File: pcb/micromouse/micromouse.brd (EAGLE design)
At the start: 80 x 115 mm, 66 parts, among them IC1 LM2575-5.0WU-(TR), IC2 LM2575-3.3WU-(TR), IC3 DSPIC33FJ64MC804-PT, IC4 L293D, Y1 7.3728MHz

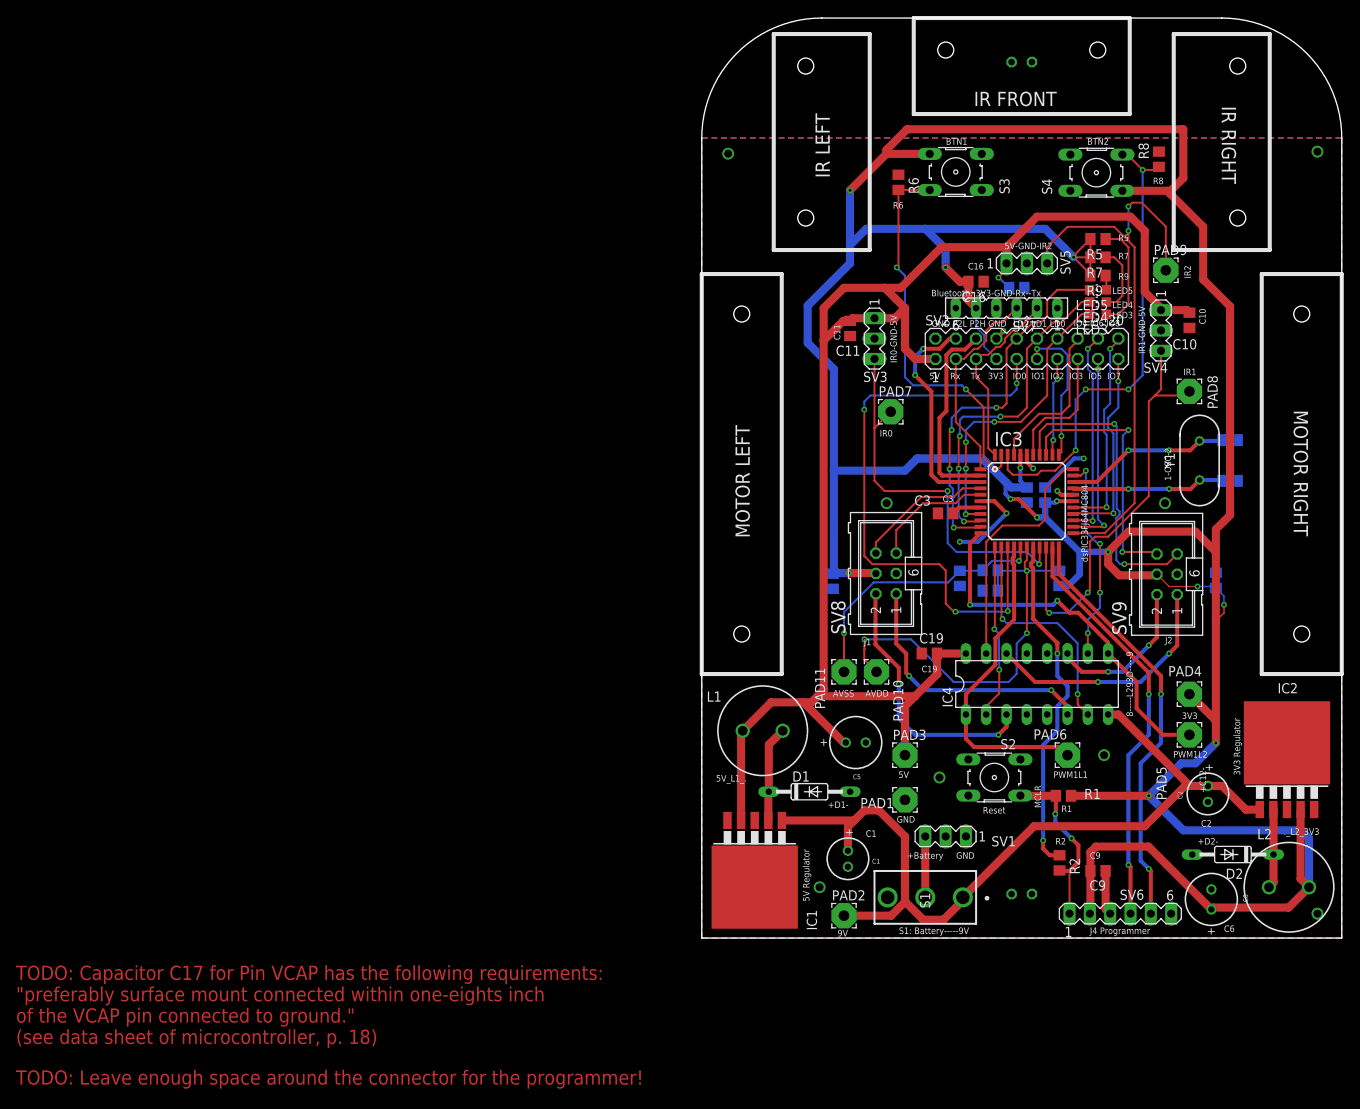
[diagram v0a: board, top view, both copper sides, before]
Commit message: Fix positioning of motor connectors.
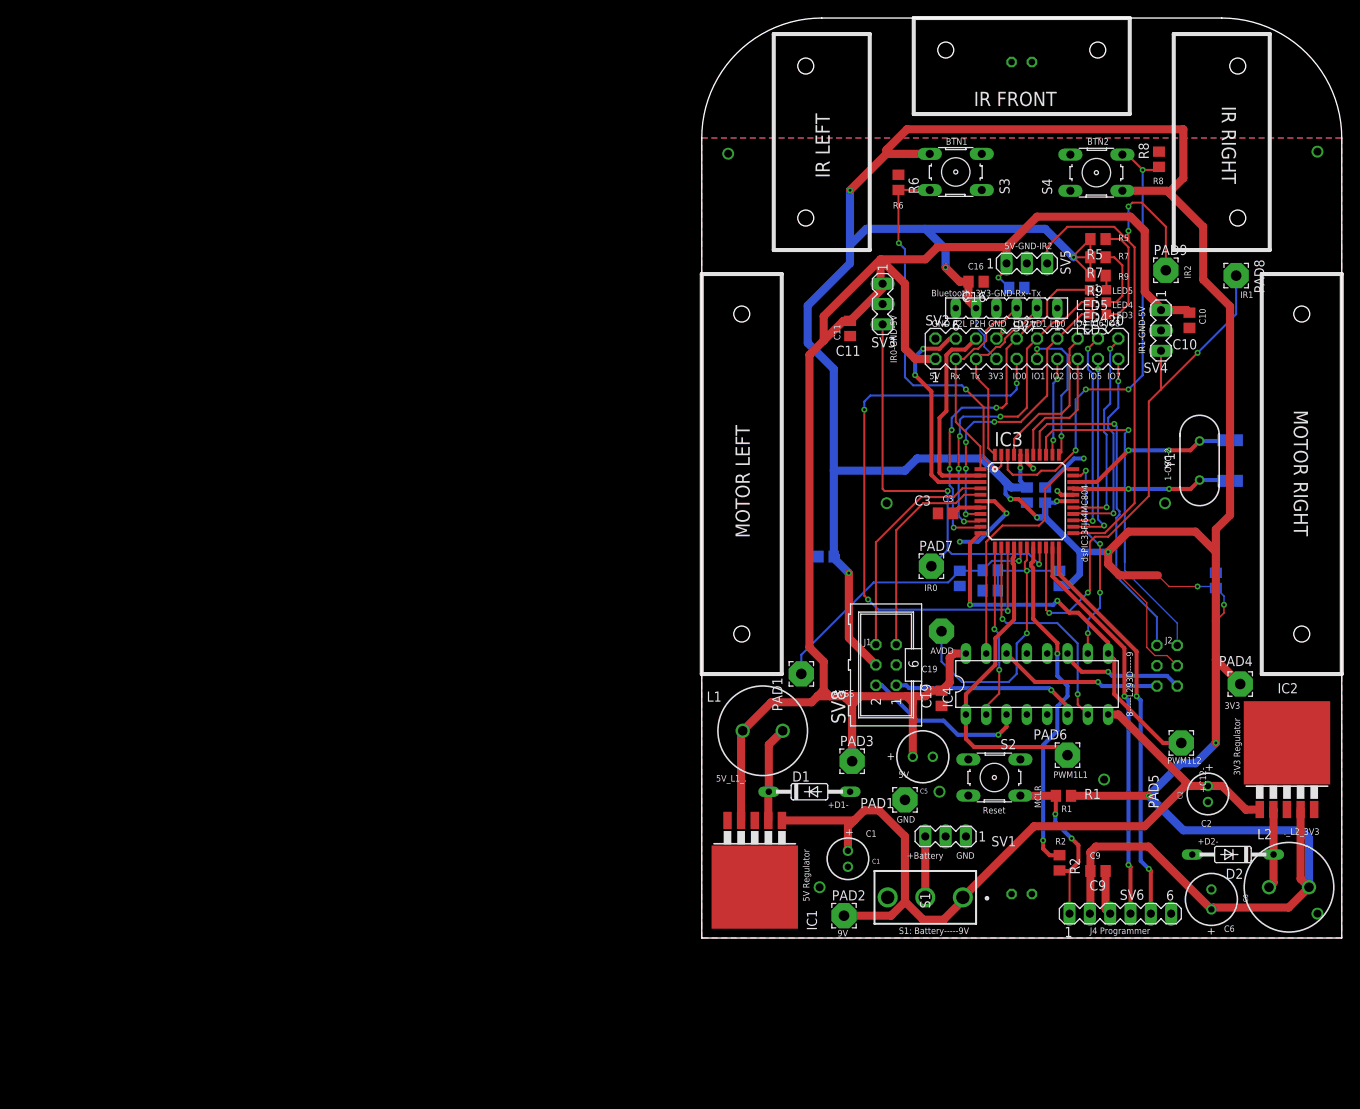
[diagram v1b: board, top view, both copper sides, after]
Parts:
- moved PAD7 20.0 mm to (28.7, 46.5)
- moved PAD8 15.6 mm to (66.8, 82.8)
- moved SV8 11.4 mm to (23.0, 34.1)
- moved SV9 11.4 mm to (58.2, 34.0), flipped to the bottom
- moved PAD10 9.58 mm to (30.0, 38.4), flipped to the bottom
- moved C5 8.57 mm to (27.6, 22.7)
- moved PAD3 6.65 mm to (18.8, 22.1)
- moved PAD4 6.48 mm to (67.3, 31.8)
- moved C19 5.79 mm to (30.0, 30.0), turned to 90 degrees
- moved PAD11 5.34 mm to (12.4, 33.0)
- moved SV3 4.44 mm to (22.6, 79.2)
- moved C17 3.19 mm to (15.5, 47.7), turned to 180 degrees
- moved PAD5 1.44 mm to (59.9, 24.4)
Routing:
- net +3V3: track 458.7 -> 483.7 mm
- net IR1: track 53.7 -> 67.3 mm, vias 2 -> 3
- net M1+: track 33.1 -> 20.8 mm, vias 2 -> 1
- net +5V: track 199.9 -> 211.7 mm
- net AVDD: track 53.1 -> 41.5 mm, vias 3 -> 2
- net ENC1_B: track 15.2 -> 26.7 mm
- net ENC1_A: track 17.2 -> 28.6 mm
- net M2-: track 31.1 -> 20.5 mm, vias 2 -> 1
- net ENC2_A: track 32.8 -> 42.7 mm, vias 2 -> 1
- net M1-: track 33.3 -> 23.5 mm, vias 2 -> 1
- net ENC2_B: track 38.4 -> 42.9 mm, vias 2 -> 1
- net IR0: track 48.9 -> 53.3 mm
- net M2+: track 19.5 -> 15.7 mm, vias 2 -> 1
- net AVSS: track 33.7 -> 36.2 mm, vias 2 -> 1
- net PGED1: track 51.9 -> 49.8 mm
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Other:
- board text added: "TODO: Capacitor C3 for Pin VCAP has the following requirements: "preferably surface mount connected within one-eights inch of the VCAP pin connected to ground." (see data sheet of microcontroller, p. 18)"
- board text removed: "TODO: Capacitor C17 for Pin VCAP has the following requirements: "preferably surface mount connected within one-eights inch of the VCAP pin connected to ground." (see data sheet of microcontroller, p. 18)"

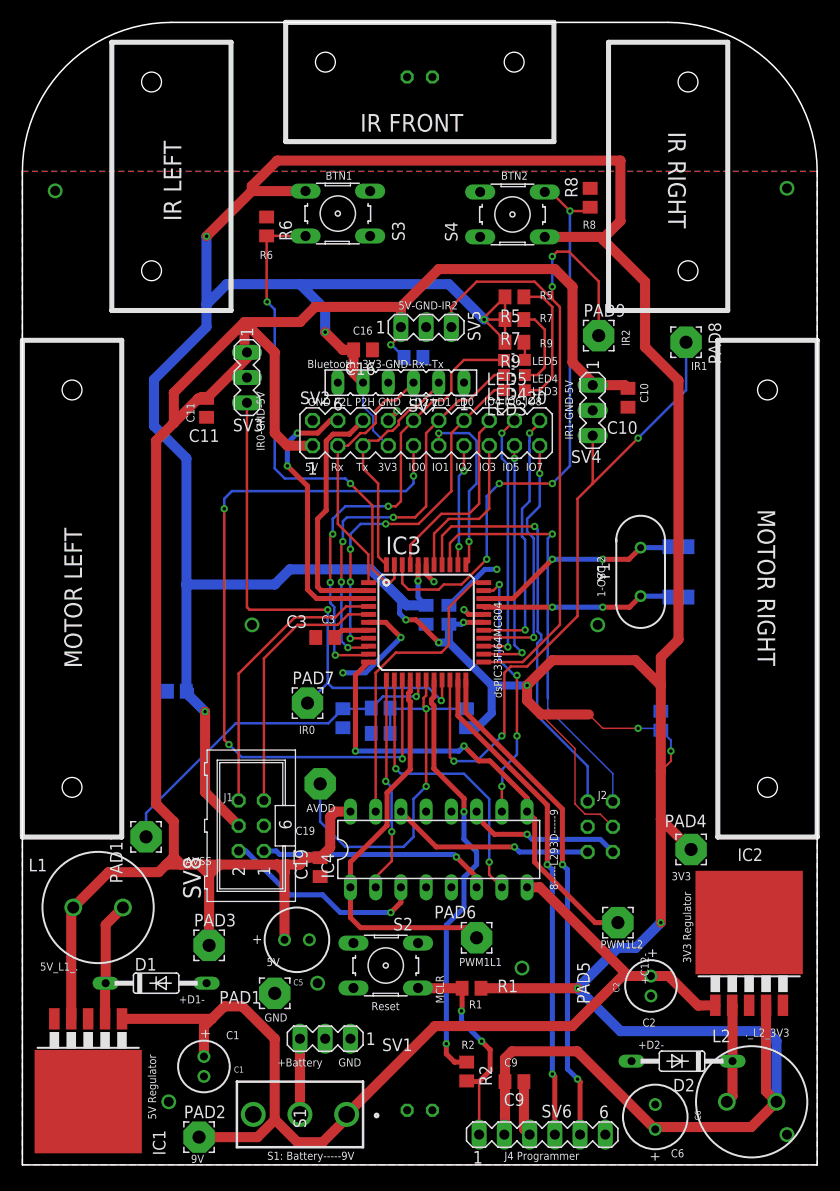
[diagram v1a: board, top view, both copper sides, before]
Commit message: Fixed ground plate isolation distance, mounting holes and errors
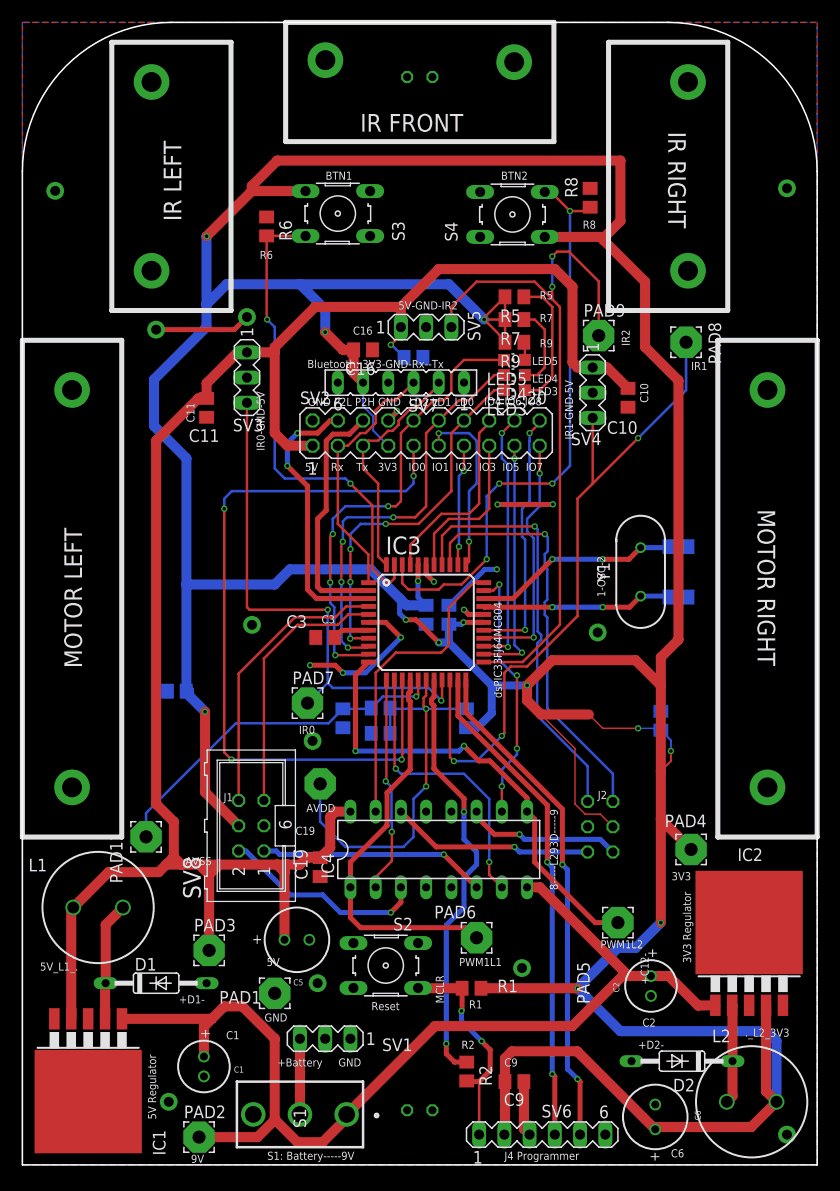
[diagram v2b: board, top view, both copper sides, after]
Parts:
- PAD1: value (none) -> TEST_GND
- PAD10: value (none) -> TEST_AVDD
- PAD11: value (none) -> TEST_AVSS
- PAD2: value (none) -> TEST_9V
- PAD3: value (none) -> TEST_5V
- PAD4: value (none) -> TEST_3V3
- PAD5: value (none) -> TEST_PWM1L2
- PAD6: value (none) -> TEST_PWM1L1
- PAD7: value (none) -> TEST_IR0
- PAD8: value (none) -> TEST_IR1
- PAD9: value (none) -> TEST_IR2
- moved SV4 1.78 mm to (57.4, 77.7)
- moved PAD3 0.51 mm to (18.8, 21.6)
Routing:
- net GND: track 28.7 -> 47.5 mm, vias 14 -> 30
- net +5V: track 211.7 -> 193.9 mm
- net IR1: track 67.3 -> 69.1 mm
- net IO0: track 74.4 -> 75.2 mm
- net M1-: track 23.5 -> 22.9 mm

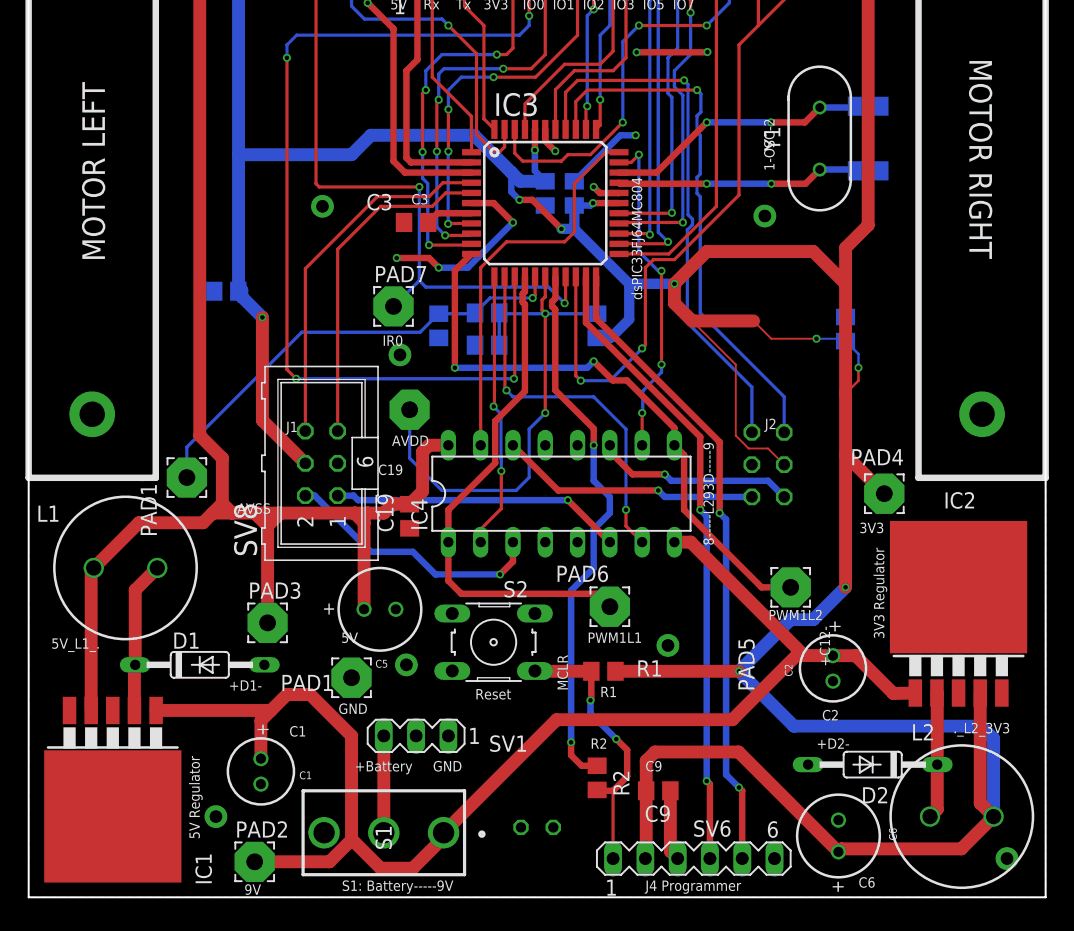
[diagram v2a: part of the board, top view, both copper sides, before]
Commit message: Almost final steps of PCB, before moving the oscillator
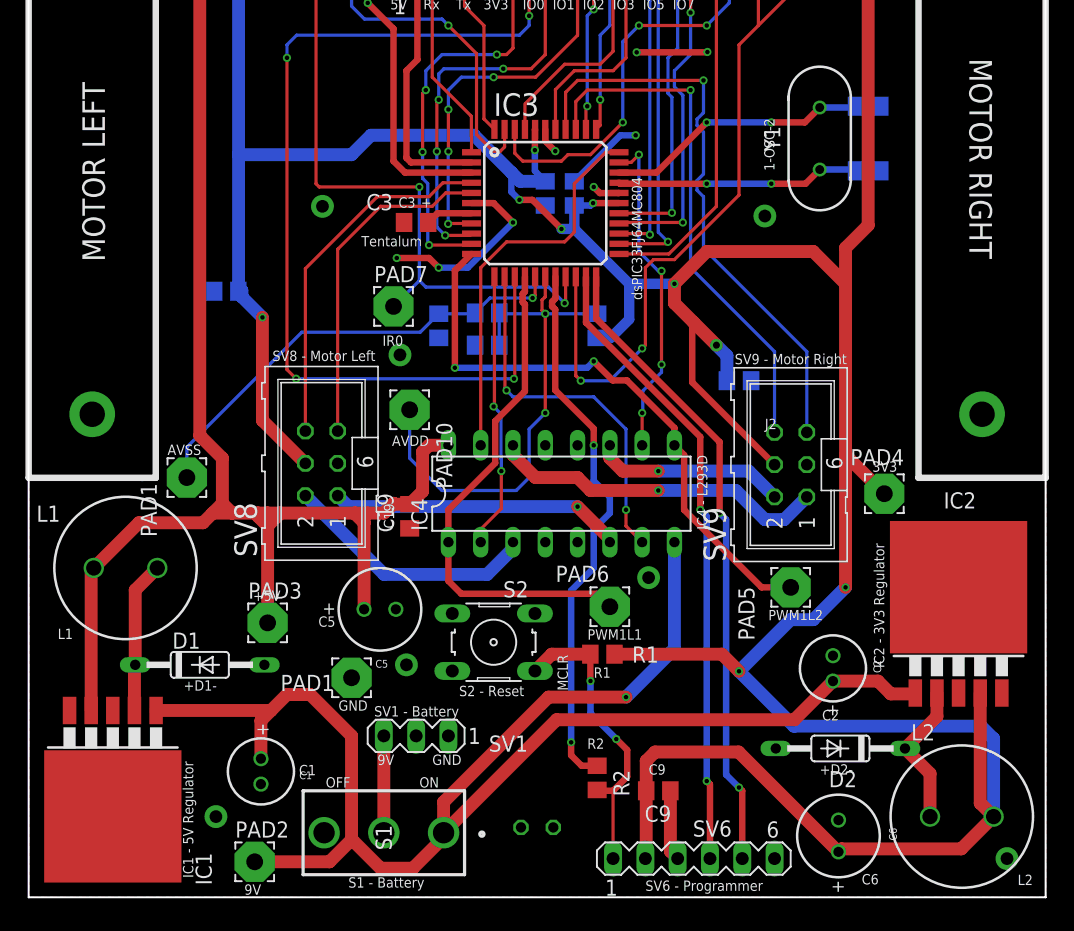
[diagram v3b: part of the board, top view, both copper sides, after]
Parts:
- moved C18 9.32 mm to (55.9, 40.6), turned to 0 degrees
- moved D2 2.84 mm to (63.9, 11.7)
- moved SV9 1.78 mm to (59.9, 34.0), flipped to the top
- moved R1 1.35 mm to (45.1, 19.1)
- turned C2 to 270 degrees
- flipped PAD10 to the top
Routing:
- net +9V: track 105.4 -> 123.9 mm, vias 0 -> 1
- net +3V3: track 483.7 -> 469.2 mm, vias 13 -> 12
- net M2-: track 20.5 -> 26.7 mm
- net ENC2_B: track 42.9 -> 46.0 mm
- net N_MCLR: track 22.2 -> 24.0 mm
- net N$8: track 9.97 -> 11.6 mm
- net ENC2_A: track 42.3 -> 41.3 mm
- net M1+: track 20.8 -> 20.2 mm, vias 1 -> 0
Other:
- board text added: "+"
- board text added: "+5V"
- board text added: "C5"
- board text added: "Capacitor C3 for Pin VCAP has the following requirements: "preferably surface mount connected within one-eights inch of the VCAP pin connected to ground." (see data sheet of microcontroller, p. 18)"
- board text added: "IC1 - 5V Regulator"
- board text added: "IC2 - 3V3 Regulator"
- board text added: "IC4 - L293D"
- board text added: "L1"
- board text added: "L2"
- board text added: "OFF"
- board text added: "ON"
- board text added: "S1 - Battery"
- board text added: "S2 - Reset"
- board text added: "SV1 - Battery"
- board text added: "SV6 - Programmer"
- board text added: "SV8 - Motor Left"
- board text added: "SV9 - Motor Right"
- board text added: "Tentalum"
- board text removed: "+Battery GND"
- board text removed: "+C12-"
- board text removed: "._L2_3V3"
- board text removed: "3V3 Regulator"
- board text removed: "5V"
- board text removed: "5V Regulator"
- board text removed: "5V_L1_."
- board text removed: "8-----L293D-----9"
- board text removed: "J1"
- board text removed: "J4 Programmer"
- board text removed: "Reset"
- board text removed: "S1: Battery-----9V"
- board text removed: "TODO: Capacitor C3 for Pin VCAP has the following requirements: "preferably surface mount connected within one-eights inch of the VCAP pin connected to ground." (see data sheet of microcontroller, p. 18)"
- board text removed: "TODO: Leave enough space around the connector for the programmer!"
